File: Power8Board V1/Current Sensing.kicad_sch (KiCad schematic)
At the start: 24 parts, among them U12 ADS1015IDGS, U13 ADS1015IDGS

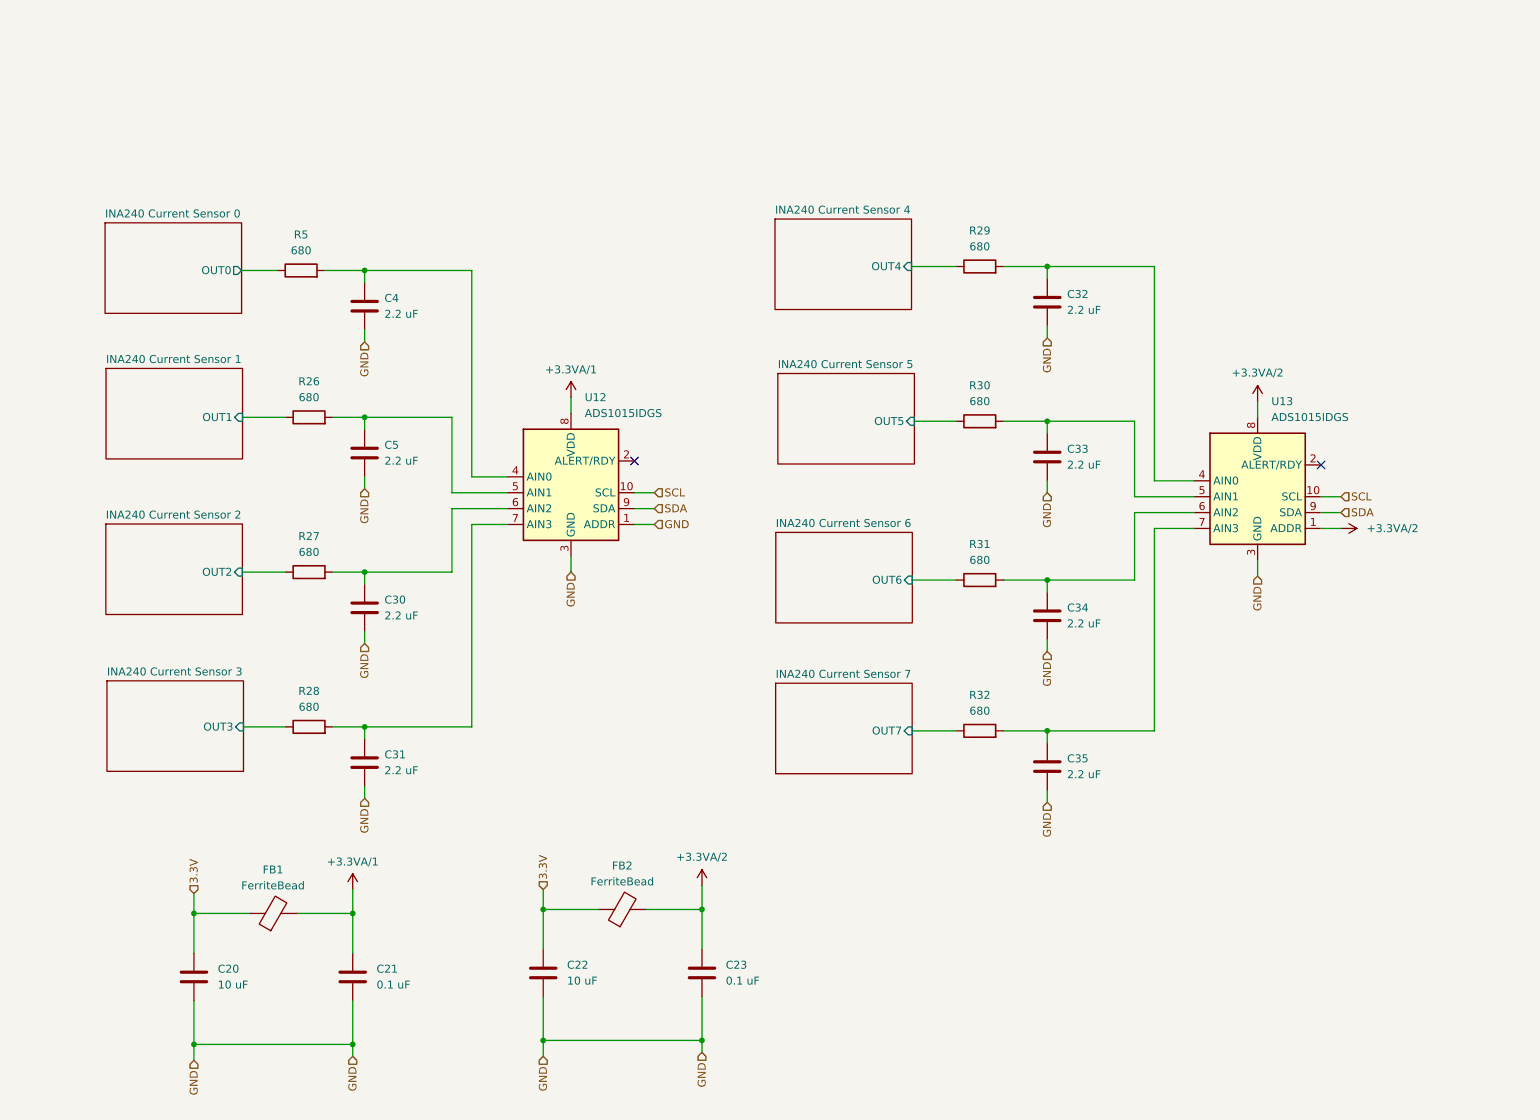
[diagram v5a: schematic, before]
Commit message: Added boxes in schematic for organization.
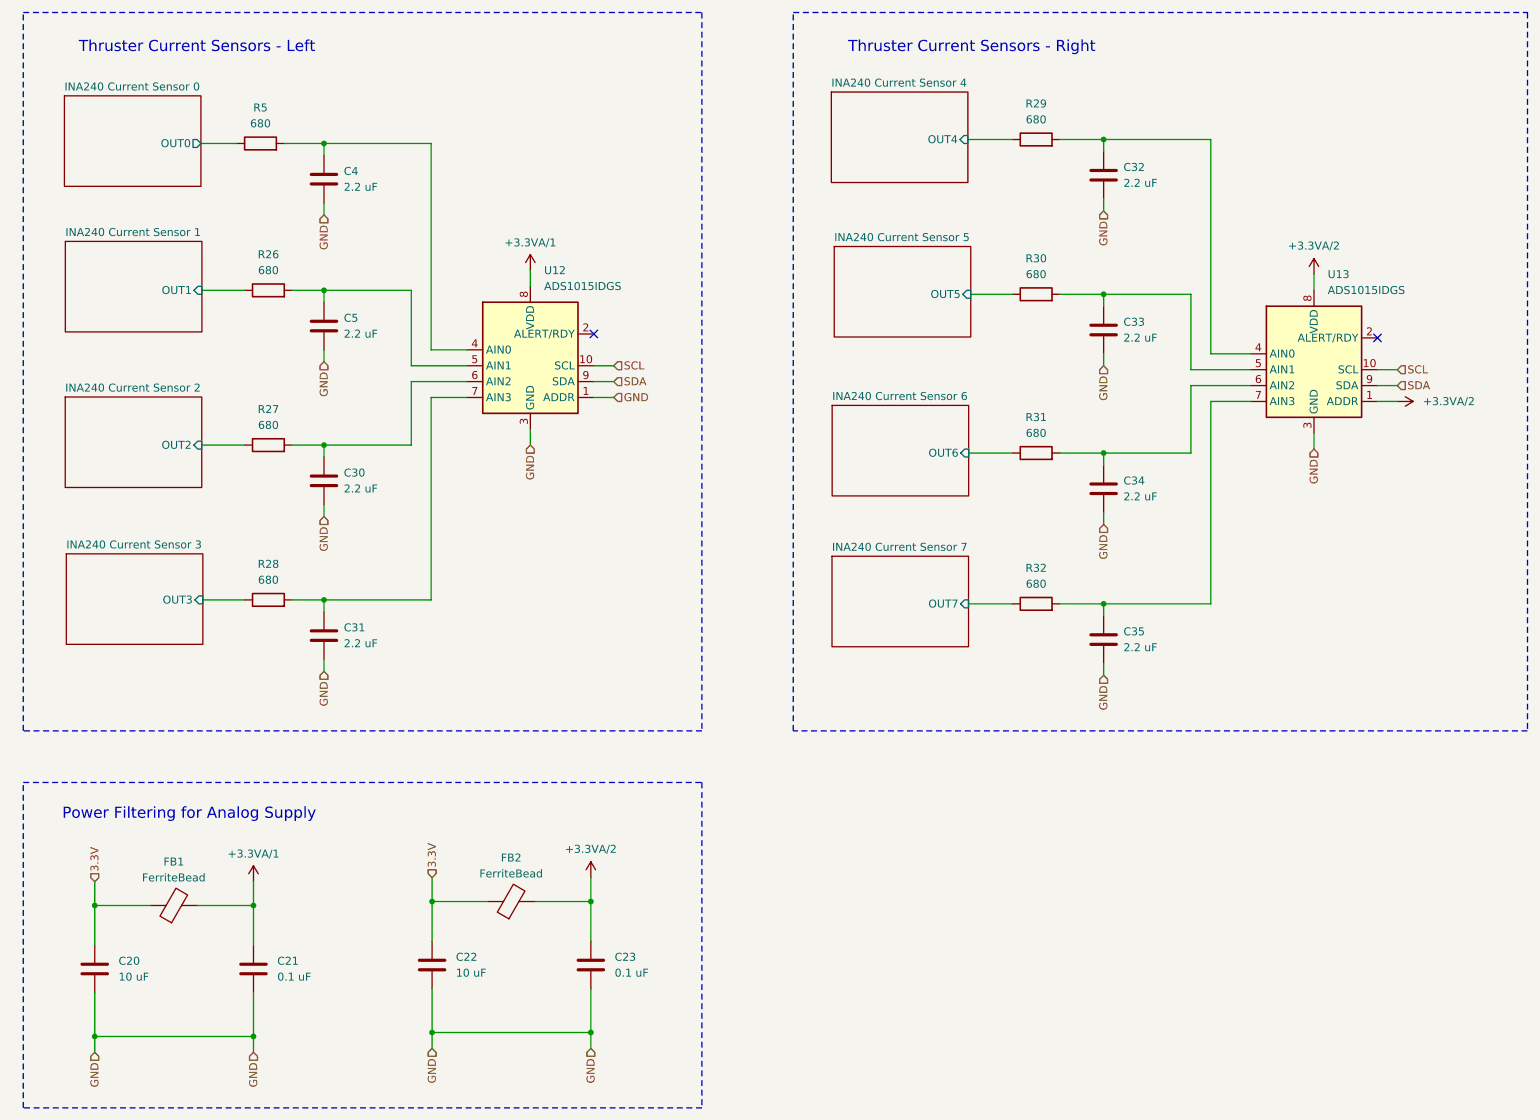
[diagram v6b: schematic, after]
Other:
- note added: "Power Filtering for Analog Supply"
- note added: "Thruster Current Sensors - Left"
- note added: "Thruster Current Sensors - Right"
- moved on the sheet: C20, C21, C22, C23, C30, C31, C32, C33, C34, C35, C4, C5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

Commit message: Moved current sensor schematics to Current Sensor folder.
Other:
- sheet INA240 Current Sensor 0: file INA240 Current Sensor 0.kicad_sch -> Current Sensors/INA240 Current Sensor 0.kicad_sch
- sheet INA240 Current Sensor 1: file INA240 Current Sensor 1.kicad_sch -> Current Sensors/INA240 Current Sensor 1.kicad_sch
- sheet INA240 Current Sensor 2: file INA240 Current Sensor 2.kicad_sch -> Current Sensors/INA240 Current Sensor 2.kicad_sch
- sheet INA240 Current Sensor 3: file INA240 Current Sensor 3.kicad_sch -> Current Sensors/INA240 Current Sensor 3.kicad_sch
- sheet INA240 Current Sensor 4: file INA240 Current Sensor 4.kicad_sch -> Current Sensors/INA240 Current Sensor 4.kicad_sch
- sheet INA240 Current Sensor 5: file INA240 Current Sensor 5.kicad_sch -> Current Sensors/INA240 Current Sensor 5.kicad_sch
- sheet INA240 Current Sensor 6: file INA240 Current Sensor 6.kicad_sch -> Current Sensors/INA240 Current Sensor 6.kicad_sch
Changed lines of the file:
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@@
 			)
 		)
-		(property "Sheetfile" "INA240 Current Sensor 5.kicad_sch"
+		(property "Sheetfile" "Current Sensors/INA240 Current Sensor 5.kicad_sch"
 			(at 158.3182 69.0122 0)
 			(effects
@@
 			)
 		)
-		(property "Sheetfile" "INA240 Current Sensor 6.kicad_sch"
+		(property "Sheetfile" "Current Sensors/INA240 Current Sensor 6.kicad_sch"
 			(at 157.988 94.4376 0)
 			(effects
@@
 			)
 		)
-		(property "Sheetfile" "INA240 Current Sensor 4.kicad_sch"
+		(property "Sheetfile" "Current Sensors/INA240 Current Sensor 4.kicad_sch"
 			(at 157.861 44.298 0)
 			(effects
@@
 			)
 		)
-		(property "Sheetfile" "INA240 Current Sensor 1.kicad_sch"
+		(property "Sheetfile" "Current Sensors/INA240 Current Sensor 1.kicad_sch"
 			(at 35.306 68.1994 0)
 			(effects
@@
 			)
 		)
-		(property "Sheetfile" "INA240 Current Sensor 0.kicad_sch"
+		(property "Sheetfile" "Current Sensors/INA240 Current Sensor 0.kicad_sch"
 			(at 35.1536 44.9076 0)
 			(effects
@@
 			)
 		)
-		(property "Sheetfile" "INA240 Current Sensor 2.kicad_sch"
+		(property "Sheetfile" "Current Sensors/INA240 Current Sensor 2.kicad_sch"
 			(at 35.2806 93.0914 0)
 			(effects
@@
 			)
 		)
-		(property "Sheetfile" "INA240 Current Sensor 3.kicad_sch"
+		(property "Sheetfile" "Current Sensors/INA240 Current Sensor 3.kicad_sch"
 			(at 35.4584 118.1866 0)
 			(effects

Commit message: Added non KiCad standard components in Components folder.
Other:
- sheet INA240 Current Sensor 7: file INA240 Current Sensor 7.kicad_sch -> Current Sensors/INA240 Current Sensor 7.kicad_sch
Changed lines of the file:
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@@
 			)
 		)
-		(property "Sheetfile" "INA240 Current Sensor 7.kicad_sch"
+		(property "Sheetfile" "Current Sensors/INA240 Current Sensor 7.kicad_sch"
 			(at 157.9626 118.5676 0)
 			(effects
